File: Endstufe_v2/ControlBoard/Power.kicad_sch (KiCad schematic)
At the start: 19 parts, among them J1 Conn_01x02_Pin, J3 DNP, U1 TPS62933, U5 NVTFWS014P04M8LTAG, U6 1SMA5927A

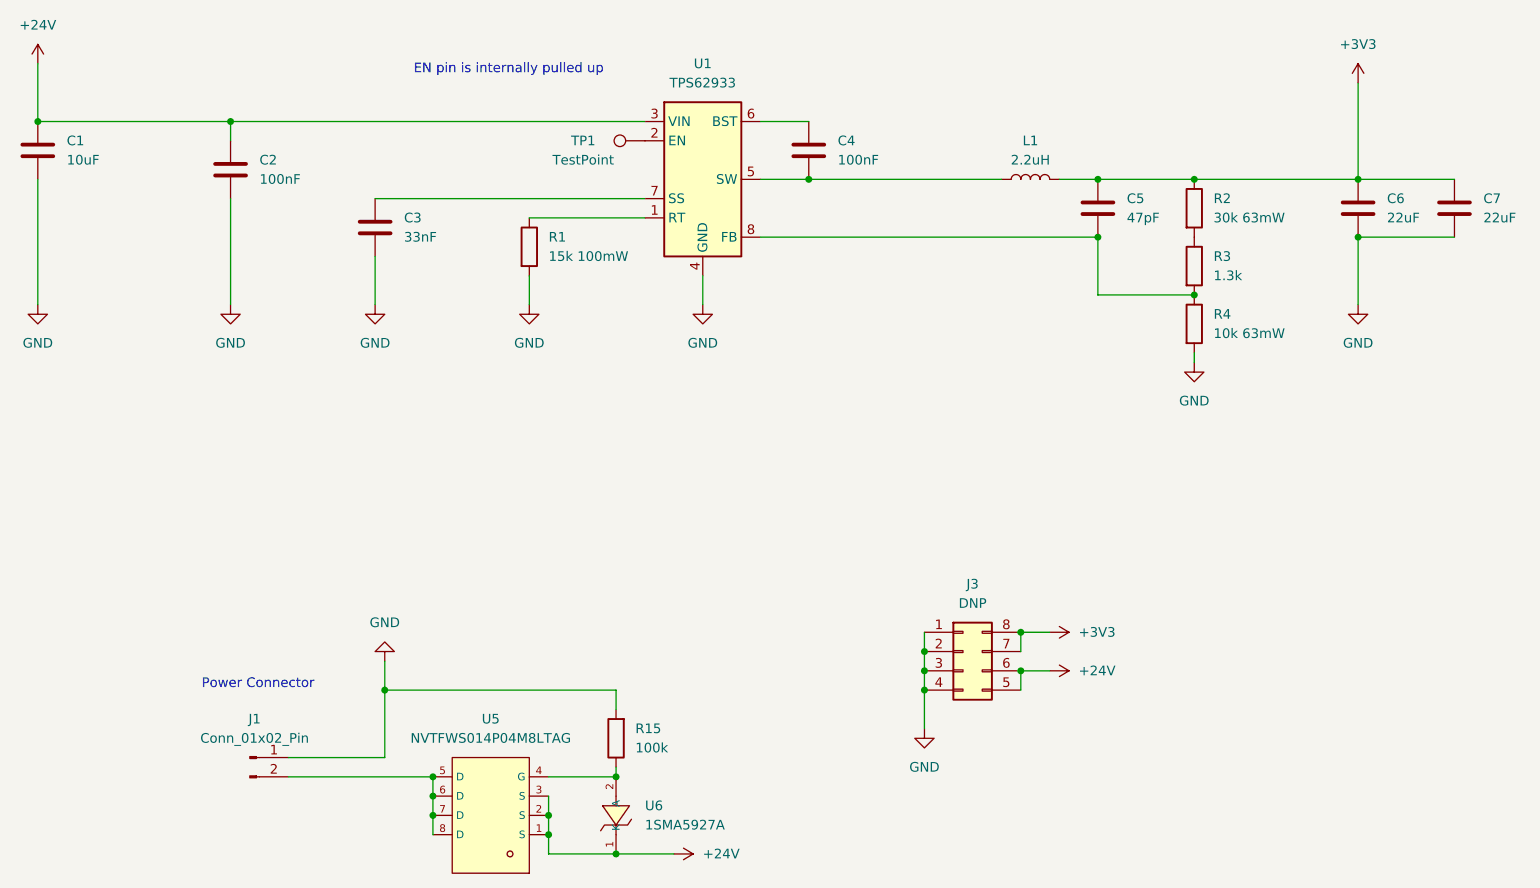
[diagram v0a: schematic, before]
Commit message: Added ADAU1962A DAC schematic
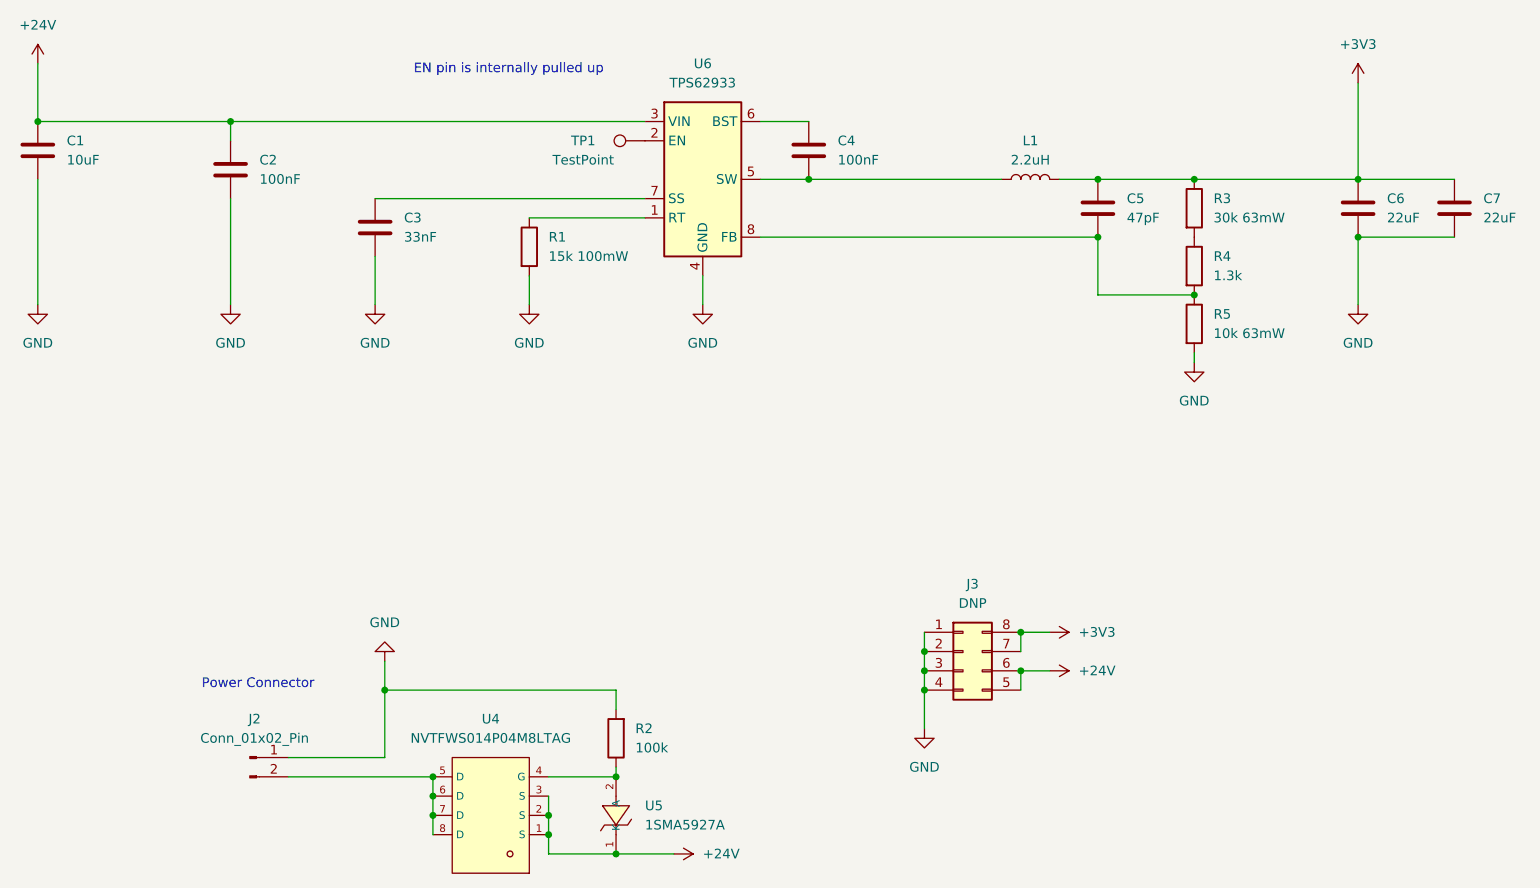
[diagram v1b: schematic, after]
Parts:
- renumbered J1 to J2, R15 to R2, R2 to R3, R3 to R4, R4 to R5, U5 to U4, U6 to U5, U1 to U6
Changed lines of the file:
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@@
 		(dnp no)
 		(fields_autoplaced yes)
-		(property "Reference" "#PWR03"
+		(property "Reference" "#PWR07"
 			(at 81.28 99.06 0)
 			(effects
@@
 			(project "ControlBoard"
 				(path "/4f887f51-77c1-41d4-a3eb-45d362caffe1/59ccf622-7ab8-4470-8173-c390bde56426"
-					(reference "#PWR03")
+					(reference "#PWR07")
 					(unit 1)
 				)
@@
 		(dnp no)
 		(fields_autoplaced yes)
-		(property "Reference" "R4"
+		(property "Reference" "R5"
 			(at 210.82 93.98 0)
 			(effects
@@
 			(project "ControlBoard"
 				(path "/4f887f51-77c1-41d4-a3eb-45d362caffe1/59ccf622-7ab8-4470-8173-c390bde56426"
-					(reference "R4")
+					(reference "R5")
 					(unit 1)
 				)
@@
 		(dnp no)
 		(fields_autoplaced yes)
-		(property "Reference" "#PWR04"
+		(property "Reference" "#PWR08"
 			(at 100.33 99.06 0)
 			(effects
@@
 			(project "ControlBoard"
 				(path "/4f887f51-77c1-41d4-a3eb-45d362caffe1/59ccf622-7ab8-4470-8173-c390bde56426"
-					(reference "#PWR04")
+					(reference "#PWR08")
 					(unit 1)
 				)
@@
 		(dnp no)
 		(fields_autoplaced yes)
-		(property "Reference" "J1"
+		(property "Reference" "J2"
 			(at 84.455 147.32 0)
 			(effects
@@
 			(project "ControlBoard"
 				(path "/4f887f51-77c1-41d4-a3eb-45d362caffe1/59ccf622-7ab8-4470-8173-c390bde56426"
-					(reference "J1")
+					(reference "J2")
 					(unit 1)
 				)
@@
 		(dnp no)
 		(fields_autoplaced yes)
-		(property "Reference" "#PWR011"
+		(property "Reference" "#PWR018"
 			(at 229.87 99.06 0)
 			(effects
@@
 			(project "ControlBoard"
 				(path "/4f887f51-77c1-41d4-a3eb-45d362caffe1/59ccf622-7ab8-4470-8173-c390bde56426"
-					(reference "#PWR011")
+					(reference "#PWR018")
 					(unit 1)
 				)
@@
 		(dnp no)
 		(fields_autoplaced yes)
-		(property "Reference" "#PWR05"
+		(property "Reference" "#PWR09"
 			(at 101.6 133.35 0)
 			(effects
@@
 			(project "ControlBoard"
 				(path "/4f887f51-77c1-41d4-a3eb-45d362caffe1/59ccf622-7ab8-4470-8173-c390bde56426"
-					(reference "#PWR05")
+					(reference "#PWR09")
 					(unit 1)
 				)
@@
 		(dnp no)
 		(fields_autoplaced yes)
-		(property "Reference" "#PWR09"
+		(property "Reference" "#PWR016"
 			(at 208.28 106.68 0)
 			(effects
@@
 			(project "ControlBoard"
 				(path "/4f887f51-77c1-41d4-a3eb-45d362caffe1/59ccf622-7ab8-4470-8173-c390bde56426"
-					(reference "#PWR09")
+					(reference "#PWR016")
 					(unit 1)
 				)
@@
 		(dnp no)
 		(fields_autoplaced yes)
-		(property "Reference" "R2"
+		(property "Reference" "R3"
 			(at 210.82 78.74 0)
 			(effects
@@
 			(project "ControlBoard"
 				(path "/4f887f51-77c1-41d4-a3eb-45d362caffe1/59ccf622-7ab8-4470-8173-c390bde56426"
-					(reference "R2")
+					(reference "R3")
 					(unit 1)
 				)
@@
 		(dnp no)
 		(fields_autoplaced yes)
-		(property "Reference" "#PWR02"
+		(property "Reference" "#PWR06"
 			(at 55.88 99.06 0)
 			(effects
@@
 			(project "ControlBoard"
 				(path "/4f887f51-77c1-41d4-a3eb-45d362caffe1/59ccf622-7ab8-4470-8173-c390bde56426"
-					(reference "#PWR02")
+					(reference "#PWR06")
 					(unit 1)
 				)
@@
 		(dnp no)
 		(fields_autoplaced yes)
-		(property "Reference" "#PWR06"
+		(property "Reference" "#PWR011"
 			(at 135.89 165.1 0)
 			(effects
@@
 			(project "ControlBoard"
 				(path "/4f887f51-77c1-41d4-a3eb-45d362caffe1/59ccf622-7ab8-4470-8173-c390bde56426"
-					(reference "#PWR06")
+					(reference "#PWR011")
 					(unit 1)
 				)
@@
 		(dnp no)
 		(fields_autoplaced yes)
-		(property "Reference" "#PWR010"
+		(property "Reference" "#PWR017"
 			(at 229.87 67.31 0)
 			(effects
@@
 			(project "ControlBoard"
 				(path "/4f887f51-77c1-41d4-a3eb-45d362caffe1/59ccf622-7ab8-4470-8173-c390bde56426"
-					(reference "#PWR010")
+					(reference "#PWR017")
 					(unit 1)
 				)
@@
 		(dnp no)
 		(fields_autoplaced yes)
-		(property "Reference" "#PWR08"
+		(property "Reference" "#PWR012"
 			(at 143.51 99.06 0)
 			(effects
@@
 			(project "ControlBoard"
 				(path "/4f887f51-77c1-41d4-a3eb-45d362caffe1/59ccf622-7ab8-4470-8173-c390bde56426"
-					(reference "#PWR08")
+					(reference "#PWR012")
 					(unit 1)
 				)
@@
 		(dnp no)
 		(fields_autoplaced yes)
-		(property "Reference" "#PWR022"
+		(property "Reference" "#PWR014"
 			(at 185.42 135.89 0)
 			(effects
@@
 			(project "ControlBoard"
 				(path "/4f887f51-77c1-41d4-a3eb-45d362caffe1/59ccf622-7ab8-4470-8173-c390bde56426"
-					(reference "#PWR022")
+					(reference "#PWR014")
 					(unit 1)
 				)
@@
 		(dnp no)
 		(fields_autoplaced yes)
-		(property "Reference" "R3"
+		(property "Reference" "R4"
 			(at 210.82 86.36 0)
 			(effects
@@
 			(project "ControlBoard"
 				(path "/4f887f51-77c1-41d4-a3eb-45d362caffe1/59ccf622-7ab8-4470-8173-c390bde56426"
-					(reference "R3")
+					(reference "R4")
 					(unit 1)
 				)
@@
 		(on_board yes)
 		(dnp no)
-		(property "Reference" "U5"
+		(property "Reference" "U4"
 			(at 115.57 147.32 0)
 			(effects
@@
 			(project "ControlBoard"
 				(path "/4f887f51-77c1-41d4-a3eb-45d362caffe1/59ccf622-7ab8-4470-8173-c390bde56426"
-					(reference "U5")
+					(reference "U4")
 					(unit 1)
 				)
@@
 		(dnp no)
 		(fields_autoplaced yes)
-		(property "Reference" "R15"
+		(property "Reference" "R2"
 			(at 134.62 148.5899 0)
 			(effects
@@
 			(project "ControlBoard"
 				(path "/4f887f51-77c1-41d4-a3eb-45d362caffe1/59ccf622-7ab8-4470-8173-c390bde56426"
-					(reference "R15")
+					(reference "R2")
 					(unit 1)
 				)
@@
 		(dnp no)
 		(fields_autoplaced yes)
-		(property "Reference" "#PWR07"
+		(property "Reference" "#PWR010"
 			(at 120.65 99.06 0)
 			(effects
@@
 			(project "ControlBoard"
 				(path "/4f887f51-77c1-41d4-a3eb-45d362caffe1/59ccf622-7ab8-4470-8173-c390bde56426"
-					(reference "#PWR07")
+					(reference "#PWR010")
 					(unit 1)
 				)
@@
 		(dnp no)
 		(fields_autoplaced yes)
-		(property "Reference" "U6"
+		(property "Reference" "U5"
 			(at 135.89 158.7499 90)
 			(effects
@@
 			(project "ControlBoard"
 				(path "/4f887f51-77c1-41d4-a3eb-45d362caffe1/59ccf622-7ab8-4470-8173-c390bde56426"
-					(reference "U6")
+					(reference "U5")
 					(unit 1)
 				)
@@
 		(dnp no)
 		(fields_autoplaced yes)
-		(property "Reference" "#PWR020"
+		(property "Reference" "#PWR013"
 			(at 172.72 154.94 0)
 			(effects
@@
 			(project "ControlBoard"
 				(path "/4f887f51-77c1-41d4-a3eb-45d362caffe1/59ccf622-7ab8-4470-8173-c390bde56426"
-					(reference "#PWR020")
+					(reference "#PWR013")
 					(unit 1)
 				)
@@
 		(dnp no)
 		(fields_autoplaced yes)
-		(property "Reference" "#PWR01"
+		(property "Reference" "#PWR05"
 			(at 55.88 64.77 0)
 			(effects
@@
 			(project "ControlBoard"
 				(path "/4f887f51-77c1-41d4-a3eb-45d362caffe1/59ccf622-7ab8-4470-8173-c390bde56426"
-					(reference "#PWR01")
+					(reference "#PWR05")
 					(unit 1)
 				)
@@
 		(dnp no)
 		(fields_autoplaced yes)
-		(property "Reference" "#PWR023"
+		(property "Reference" "#PWR015"
 			(at 185.42 140.97 0)
 			(effects
@@
 			(project "ControlBoard"
 				(path "/4f887f51-77c1-41d4-a3eb-45d362caffe1/59ccf622-7ab8-4470-8173-c390bde56426"
-					(reference "#PWR023")
+					(reference "#PWR015")
 					(unit 1)
 				)
@@
 		(dnp no)
 		(fields_autoplaced yes)
-		(property "Reference" "U1"
+		(property "Reference" "U6"
 			(at 143.51 60.96 0)
 			(effects
@@
 			(project "ControlBoard"
 				(path "/4f887f51-77c1-41d4-a3eb-45d362caffe1/59ccf622-7ab8-4470-8173-c390bde56426"
-					(reference "U1")
-					(unit 1)
-				)
+					(reference "U6")
+					(unit 1)
+				)

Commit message: Add footprints to all components
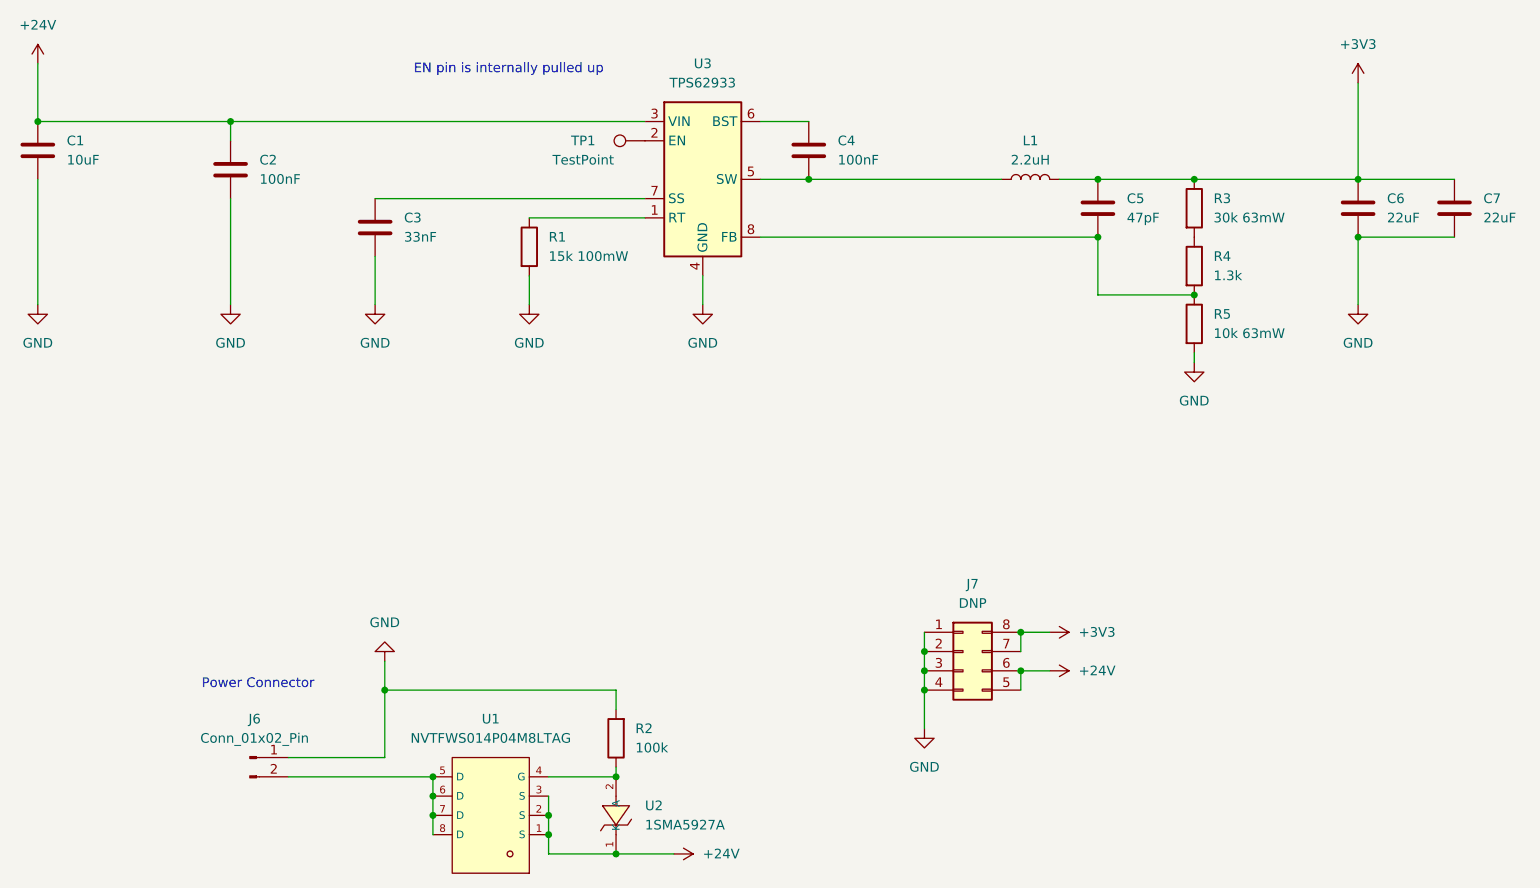
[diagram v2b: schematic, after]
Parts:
- TP1: footprint (none) -> TestPoint:TestPoint_Pad_D1.0mm
- renumbered J2 to J6, J3 to J7, U4 to U1, U5 to U2, U6 to U3
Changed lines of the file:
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@@
 		(dnp no)
 		(fields_autoplaced yes)
-		(property "Reference" "J3"
+		(property "Reference" "J7"
 			(at 179.07 129.54 0)
 			(effects
@@
 			(project "ControlBoard"
 				(path "/4f887f51-77c1-41d4-a3eb-45d362caffe1/59ccf622-7ab8-4470-8173-c390bde56426"
-					(reference "J3")
+					(reference "J7")
 					(unit 1)
 				)
@@
 		(dnp no)
 		(fields_autoplaced yes)
-		(property "Reference" "J2"
+		(property "Reference" "J6"
 			(at 84.455 147.32 0)
 			(effects
@@
 			(project "ControlBoard"
 				(path "/4f887f51-77c1-41d4-a3eb-45d362caffe1/59ccf622-7ab8-4470-8173-c390bde56426"
-					(reference "J2")
+					(reference "J6")
 					(unit 1)
 				)
@@
 			)
 		)
-		(property "Footprint" ""
+		(property "Footprint" "TestPoint:TestPoint_Pad_D1.0mm"
 			(at 135.89 66.04 0)
 			(effects
@@
 		(on_board yes)
 		(dnp no)
-		(property "Reference" "U4"
+		(property "Reference" "U1"
 			(at 115.57 147.32 0)
 			(effects
@@
 			(project "ControlBoard"
 				(path "/4f887f51-77c1-41d4-a3eb-45d362caffe1/59ccf622-7ab8-4470-8173-c390bde56426"
-					(reference "U4")
+					(reference "U1")
 					(unit 1)
 				)
@@
 		(dnp no)
 		(fields_autoplaced yes)
-		(property "Reference" "U5"
+		(property "Reference" "U2"
 			(at 135.89 158.7499 90)
 			(effects
@@
 			(project "ControlBoard"
 				(path "/4f887f51-77c1-41d4-a3eb-45d362caffe1/59ccf622-7ab8-4470-8173-c390bde56426"
-					(reference "U5")
+					(reference "U2")
 					(unit 1)
 				)
@@
 		(dnp no)
 		(fields_autoplaced yes)
-		(property "Reference" "U6"
+		(property "Reference" "U3"
 			(at 143.51 60.96 0)
 			(effects
@@
 			(project "ControlBoard"
 				(path "/4f887f51-77c1-41d4-a3eb-45d362caffe1/59ccf622-7ab8-4470-8173-c390bde56426"
-					(reference "U6")
-					(unit 1)
-				)
+					(reference "U3")
+					(unit 1)
+				)

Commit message: Fix connector footprints
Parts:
- J6: footprint Endstufe:Molex_Sabre_43160-1102_1x02_P7.49mm_Horizontal -> Connector_JST:JST_XH_B2B-XH-A_1x02_P2.50mm_Vertical; LCSC Part # - -> C158012
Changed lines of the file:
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@@
 			)
 		)
-		(property "Footprint" "Endstufe:Molex_Sabre_43160-1102_1x02_P7.49mm_Horizontal"
+		(property "Footprint" "Connector_JST:JST_XH_B2B-XH-A_1x02_P2.50mm_Vertical"
 			(at 83.82 152.4 0)
 			(effects
@@
 			)
 		)
-		(property "LCSC Part #" "-"
+		(property "LCSC Part #" "C158012"
 			(at 83.82 152.4 0)
 			(effects

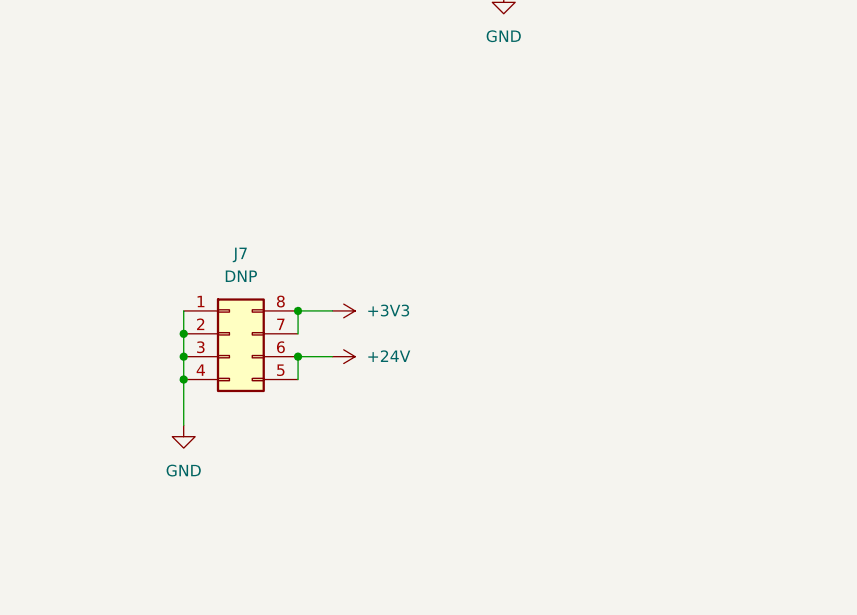
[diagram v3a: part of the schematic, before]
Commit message: Add forgotten 3V3 outputs to control board
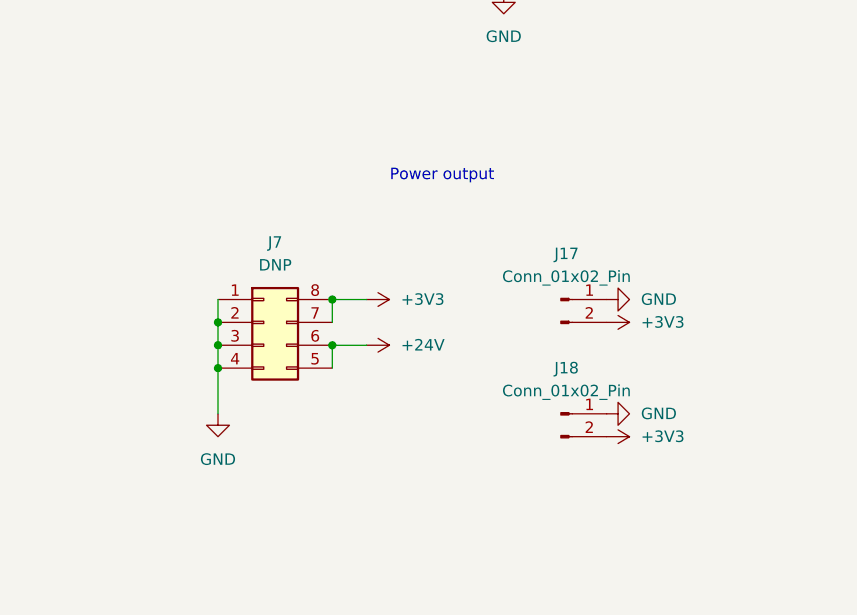
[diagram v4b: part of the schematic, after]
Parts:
- added J17, J18: Conn_01x02_Pin, Connector_JST:JST_XH_B2B-XH-A_1x02_P2.50mm_Vertical, symbol Endstufe:Conn_01x02_Pin
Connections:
- net +3V3: now also J17.2 (Pin_2), J18.2 (Pin_2)
- net GND: now also J17.1 (Pin_1), J18.1 (Pin_1)
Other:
- note added: "Power output"
- moved on the sheet: J7
